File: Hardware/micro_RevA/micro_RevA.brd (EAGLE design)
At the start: 50 x 50 mm, 22 parts, among them IC1 TLC59711, Q1 CSTCR6M00G53Z

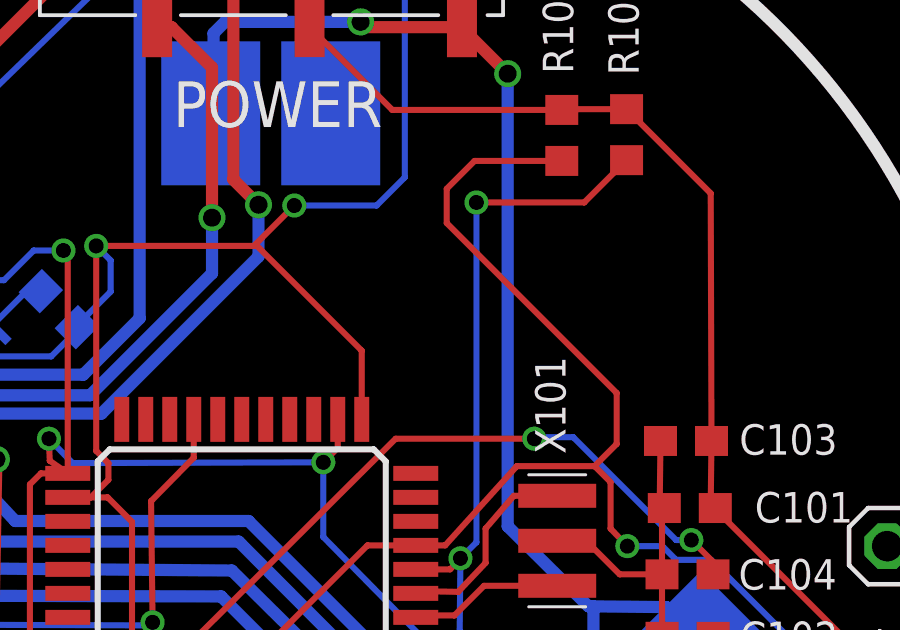
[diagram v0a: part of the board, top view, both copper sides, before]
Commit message: Added Javen's logo to everything
Still need to add plus/minus on leds before order.
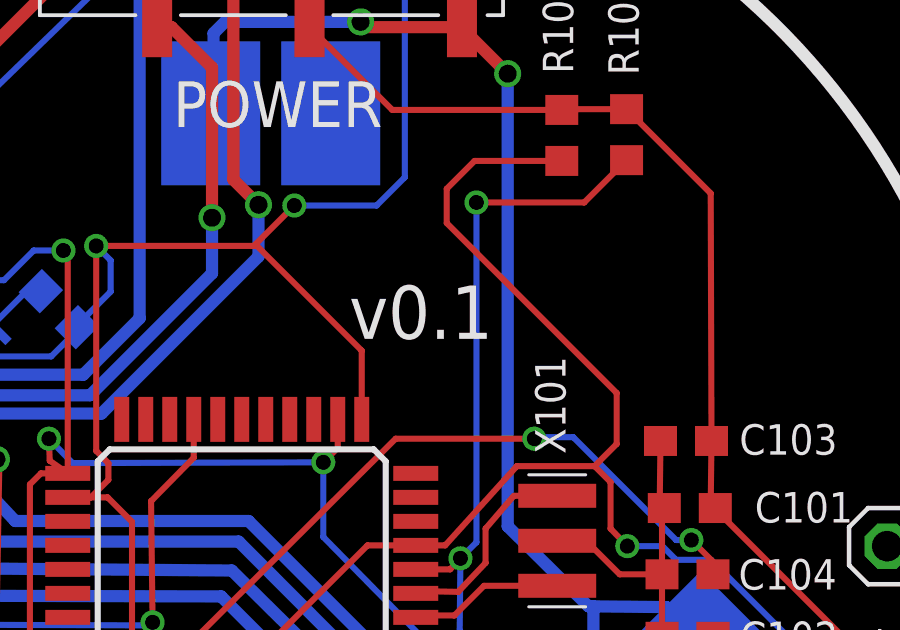
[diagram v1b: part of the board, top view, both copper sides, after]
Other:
- board text added: "v0.1"
- board text removed: "TES"

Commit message: Update of hw files
Added logo to brds, added +/- to LEDs and generated and updated gerber
files.
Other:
- outline, holes or cut-outs redrawn
- board text added: "+"
- board text added: "-"
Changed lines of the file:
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@@
 <layer number="17" name="Pads" color="2" fill="1" visible="yes" active="yes"/>
 <layer number="18" name="Vias" color="2" fill="1" visible="yes" active="yes"/>
-<layer number="19" name="Unrouted" color="6" fill="1" visible="yes" active="yes"/>
+<layer number="19" name="Unrouted" color="6" fill="1" visible="no" active="yes"/>
 <layer number="20" name="Dimension" color="6" fill="1" visible="yes" active="yes"/>
 <layer number="21" name="tPlace" color="10" fill="1" visible="yes" active="yes"/>
-<layer number="22" name="bPlace" color="3" fill="1" visible="yes" active="yes"/>
-<layer number="23" name="tOrigins" color="15" fill="1" visible="yes" active="yes"/>
-<layer number="24" name="bOrigins" color="15" fill="1" visible="yes" active="yes"/>
-<layer number="25" name="tNames" color="7" fill="1" visible="yes" active="yes"/>
-<layer number="26" name="bNames" color="7" fill="1" visible="yes" active="yes"/>
-<layer number="27" name="tValues" color="7" fill="1" visible="yes" active="yes"/>
-<layer number="28" name="bValues" color="7" fill="1" visible="yes" active="yes"/>
+<layer number="22" name="bPlace" color="13" fill="1" visible="yes" active="yes"/>
+<layer number="23" name="tOrigins" color="15" fill="1" visible="no" active="yes"/>
+<layer number="24" name="bOrigins" color="15" fill="1" visible="no" active="yes"/>
+<layer number="25" name="tNames" color="7" fill="1" visible="no" active="yes"/>
+<layer number="26" name="bNames" color="7" fill="1" visible="no" active="yes"/>
+<layer number="27" name="tValues" color="7" fill="1" visible="no" active="yes"/>
+<layer number="28" name="bValues" color="7" fill="1" visible="no" active="yes"/>
 <layer number="29" name="tStop" color="7" fill="3" visible="yes" active="yes"/>
 <layer number="30" name="bStop" color="7" fill="6" visible="yes" active="yes"/>
@@
 <layer number="109" name="fp9" color="7" fill="1" visible="no" active="yes"/>
 <layer number="110" name="fp0" color="7" fill="1" visible="no" active="yes"/>
-<layer number="111" name="LPC17xx" color="7" fill="1" visible="yes" active="yes"/>
-<layer number="112" name="tSilk" color="7" fill="1" visible="yes" active="yes"/>
-<layer number="113" name="IDFDebug" color="4" fill="1" visible="yes" active="yes"/>
-<layer number="116" name="Patch_BOT" color="9" fill="4" visible="yes" active="yes"/>
-<layer number="121" name="_tsilk" color="7" fill="1" visible="yes" active="yes"/>
-<layer number="122" name="_bsilk" color="7" fill="1" visible="yes" active="yes"/>
+<layer number="111" name="LPC17xx" color="7" fill="1" visible="no" active="yes"/>
+<layer number="112" name="tSilk" color="7" fill="1" visible="no" active="yes"/>
+<layer number="113" name="IDFDebug" color="4" fill="1" visible="no" active="yes"/>
+<layer number="116" name="Patch_BOT" color="9" fill="4" visible="no" active="yes"/>
+<layer number="121" name="_tsilk" color="7" fill="1" visible="no" active="yes"/>
+<layer number="122" name="_bsilk" color="7" fill="1" visible="no" active="yes"/>
 <layer number="123" name="tTestmark" color="7" fill="1" visible="no" active="yes"/>
 <layer number="124" name="bTestmark" color="7" fill="1" visible="no" active="yes"/>
-<layer number="125" name="_tNames" color="7" fill="1" visible="yes" active="yes"/>
-<layer number="126" name="_bNames" color="7" fill="1" visible="yes" active="yes"/>
-<layer number="127" name="_tValues" color="7" fill="1" visible="yes" active="yes"/>
-<layer number="128" name="_bValues" color="7" fill="1" visible="yes" active="yes"/>
+<layer number="125" name="_tNames" color="7" fill="1" visible="no" active="yes"/>
+<layer number="126" name="_bNames" color="7" fill="1" visible="no" active="yes"/>
+<layer number="127" name="_tValues" color="7" fill="1" visible="no" active="yes"/>
+<layer number="128" name="_bValues" color="7" fill="1" visible="no" active="yes"/>
 <layer number="131" name="tAdjust" color="7" fill="1" visible="no" active="yes"/>
 <layer number="132" name="bAdjust" color="7" fill="1" visible="no" active="yes"/>
@@
 <board>
 <plain>
-<wire x1="0" y1="0" x2="50" y2="0" width="0" layer="20"/>
-<wire x1="50" y1="0" x2="50" y2="50" width="0" layer="20"/>
-<wire x1="50" y1="50" x2="0" y2="50" width="0" layer="20"/>
-<wire x1="0" y1="50" x2="0" y2="0" width="0" layer="20"/>
+<wire x1="0" y1="25" x2="25" y2="0" width="0" layer="20" curve="90"/>
+<wire x1="25" y1="0" x2="50" y2="25" width="0" layer="20" curve="90"/>
+<wire x1="50" y1="25" x2="25" y2="50" width="0" layer="20" curve="90"/>
+<wire x1="25" y1="50" x2="0" y2="25" width="0" layer="20" curve="90"/>
 <circle x="25.0444" y="25.1206" radius="24.385321875" width="0.4064" layer="21"/>
 <text x="35.179" y="28.1686" size="1.016" layer="21" ratio="10" rot="R90">X101</text>
@@
 <rectangle x1="18.1991" y1="26.9621" x2="18.3515" y2="26.9875" layer="22" rot="R180"/>
 <rectangle x1="18.2245" y1="26.9875" x2="18.3261" y2="27.0129" layer="22" rot="R180"/>
+<text x="42" y="25" size="2" layer="22" ratio="15" rot="MR225">+</text>
+<text x="4" y="20" size="2" layer="22" ratio="15" rot="MR225">+</text>
+<text x="19" y="41" size="2" layer="22" ratio="15" rot="MR180">+</text>
+<text x="29" y="46" size="2" layer="22" ratio="15" rot="MR180">-</text>
+<text x="15" y="18" size="2" layer="22" ratio="15" rot="MR225">-</text>
+<text x="38" y="12" size="2" layer="22" ratio="15" rot="MR135">-</text>
 </plain>
 <attributes>
